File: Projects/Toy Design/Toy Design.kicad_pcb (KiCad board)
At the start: 2 copper layers, 34 parts, among them J1 Conn_01x01_Pin, J2 Conn_01x01_Pin, U1 TLV61048DBVR, U2 MCP73123, U3 NCP1117-5.0_SOT223, U4 MLX90333, U5 MLX90333, U6 MLX90333, U7 LMC6484, U8 LMC6484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

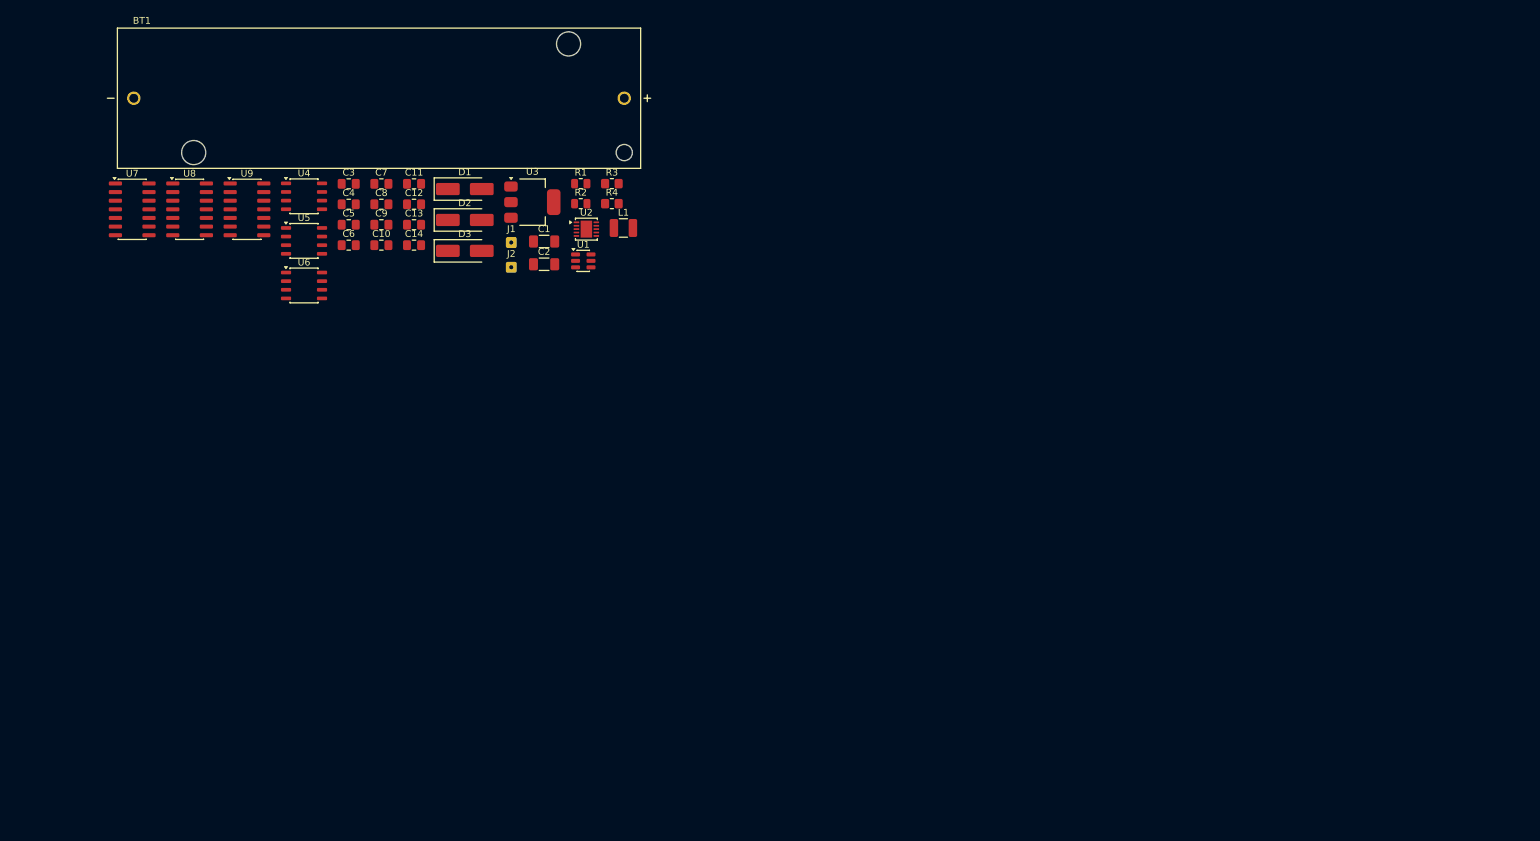
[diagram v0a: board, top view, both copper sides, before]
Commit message: Updates
Began PCB Layout and added LED controls and 3.3 to 5V level shifter
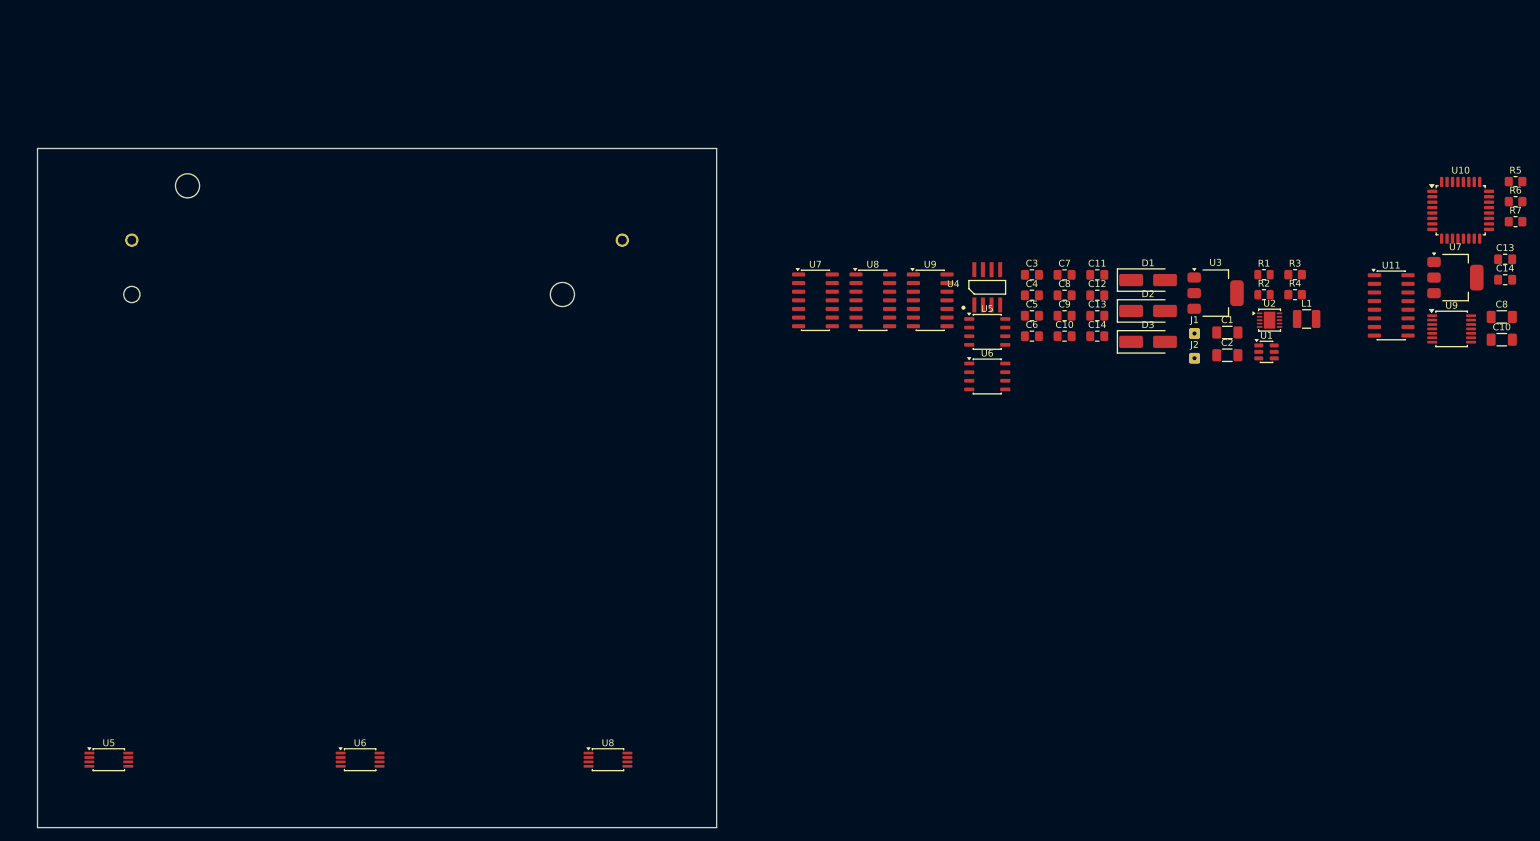
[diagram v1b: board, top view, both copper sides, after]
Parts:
- added C10: 10uF, Capacitor_SMD:C_1206_3216Metric_Pad1.33x1.80mm_HandSolder, F.Cu at (315.6, 78.2)
- added C13: 100nF, Capacitor_SMD:C_0805_2012Metric_Pad1.18x1.45mm_HandSolder, F.Cu at (316.1, 66.3)
- added C14: 100nF, Capacitor_SMD:C_0805_2012Metric_Pad1.18x1.45mm_HandSolder, F.Cu at (316.1, 69.3)
- added C8: 10uF, Capacitor_SMD:C_1206_3216Metric_Pad1.33x1.80mm_HandSolder, F.Cu at (315.6, 74.8)
- added R5: 10k, Resistor_SMD:R_0805_2012Metric_Pad1.20x1.40mm_HandSolder, F.Cu at (317.6, 54.9)
- added R6: 10k, Resistor_SMD:R_0805_2012Metric_Pad1.20x1.40mm_HandSolder, F.Cu at (317.6, 57.8)
- added R7: 10k, Resistor_SMD:R_0805_2012Metric_Pad1.20x1.40mm_HandSolder, F.Cu at (317.6, 60.8)
- added U10: STM32G030K6T6, Package_QFP:LQFP-32_7x7mm_P0.8mm, F.Cu at (309.6, 59.1)
- added U11: MCP3208-CI/SL, Package_SO:SOIC-16_3.9x9.9mm_P1.27mm, F.Cu at (299.3, 73.1)
- added U5: A1330, Package_SO:TSSOP-8_4.4x3mm_P0.65mm, F.Cu at (110.5, 140.0)
- added U6: A1330, Package_SO:TSSOP-8_4.4x3mm_P0.65mm, F.Cu at (147.5, 140.0)
- added U7: NCP1117-3.3_SOT223, Package_TO_SOT_SMD:SOT-223-3_TabPin2, F.Cu at (308.8, 69.0)
- added U8: A1330, Package_SO:TSSOP-8_4.4x3mm_P0.65mm, F.Cu at (184.0, 140.0)
- added U9: TXU0104, Package_SO:TSSOP-14_4.4x5mm_P0.65mm, F.Cu at (308.2, 76.6)
- BT1: moved to B.Cu
- U4: footprint Package_SO:JEITA_SOIC-8_3.9x4.9mm_P1.27mm -> ToyDesign:SOIC-8
- moved C1 101.5 mm to (275.2, 77.1)
- moved C10 101.5 mm to (251.2, 77.6)
- moved C2 101.5 mm to (275.2, 80.4)
- moved C3 101.5 mm to (246.4, 68.6)
- moved C4 101.5 mm to (246.4, 71.6)
- moved C5 101.5 mm to (246.4, 74.6)
- moved C6 101.5 mm to (246.4, 77.6)
- moved C7 101.5 mm to (251.2, 68.6)
- moved C8 101.5 mm to (251.2, 71.6)
- moved C9 101.5 mm to (251.2, 74.6)
- moved D1 101.5 mm to (263.5, 69.4)
- moved D2 101.5 mm to (263.5, 73.9)
- moved D3 101.5 mm to (263.5, 78.5)
- moved L1 101.5 mm to (286.9, 75.1)
- moved U7 101.5 mm to (214.5, 72.4)
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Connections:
- C12 pad 1: OUT2_U6 -> OUT_U6
- C9 pad 1: OUT1_U5 -> OUT_U5
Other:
- board outline added: 100 x 100 mm

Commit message: started pcb post led bar
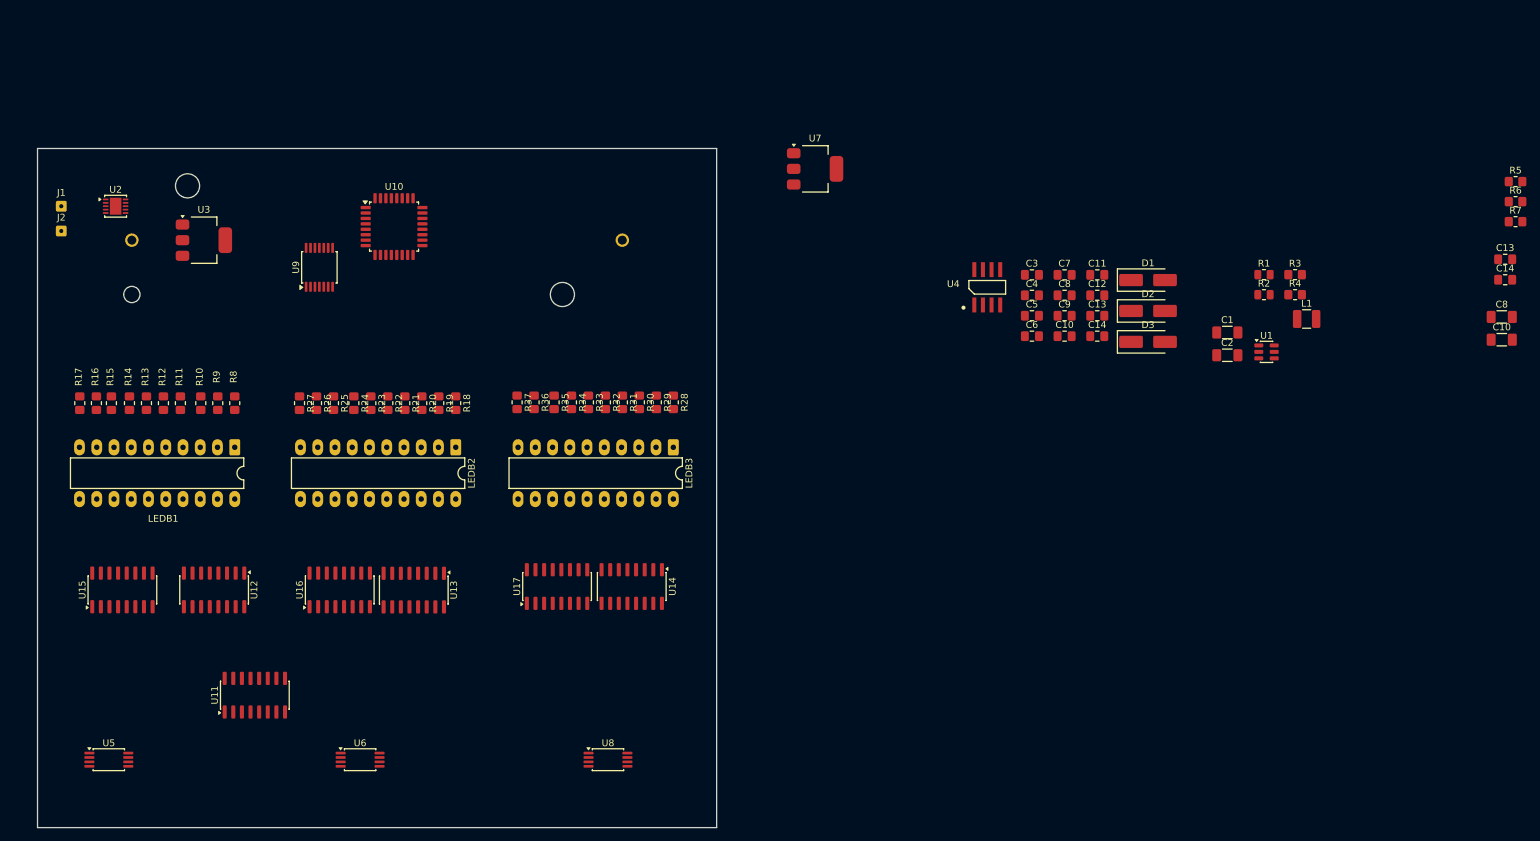
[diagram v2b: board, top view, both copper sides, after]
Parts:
- removed the U5 at (239.8, 77.0)
- removed the U6 at (239.8, 83.6)
- removed the U7 at (214.5, 72.4)
- removed the U8 at (223.0, 72.4)
- removed the U9 at (231.4, 72.4)
- added LEDB1: ~, Package_DIP:DIP-20_W7.62mm_LongPads, F.Cu at (129.0, 94.0)
- added LEDB2: ~, Package_DIP:DIP-20_W7.62mm_LongPads, F.Cu at (161.6, 94.0)
- added LEDB3: ~, Package_DIP:DIP-20_W7.62mm_LongPads, F.Cu at (193.6, 94.0)
- added R10: 1.2k, Resistor_SMD:R_0805_2012Metric_Pad1.20x1.40mm_HandSolder, F.Cu at (124.0, 87.5)
- added R11: 1.2k, Resistor_SMD:R_0805_2012Metric_Pad1.20x1.40mm_HandSolder, F.Cu at (121.0, 87.5)
- added R12: 1.2k, Resistor_SMD:R_0805_2012Metric_Pad1.20x1.40mm_HandSolder, F.Cu at (118.5, 87.5)
- added R13: 1.2k, Resistor_SMD:R_0805_2012Metric_Pad1.20x1.40mm_HandSolder, F.Cu at (116.0, 87.5)
- added R14: 1.2k, Resistor_SMD:R_0805_2012Metric_Pad1.20x1.40mm_HandSolder, F.Cu at (113.5, 87.5)
- added R15: 1.2k, Resistor_SMD:R_0805_2012Metric_Pad1.20x1.40mm_HandSolder, F.Cu at (110.9, 87.5)
- added R16: 1.2k, Resistor_SMD:R_0805_2012Metric_Pad1.20x1.40mm_HandSolder, F.Cu at (108.7, 87.5)
- added R17: 1.2k, Resistor_SMD:R_0805_2012Metric_Pad1.20x1.40mm_HandSolder, F.Cu at (106.2, 87.5)
- added R18: 1.2k, Resistor_SMD:R_0805_2012Metric_Pad1.20x1.40mm_HandSolder, F.Cu at (161.6, 87.5)
- added R19: 1.2k, Resistor_SMD:R_0805_2012Metric_Pad1.20x1.40mm_HandSolder, F.Cu at (159.1, 87.5)
- added R20: 1.2k, Resistor_SMD:R_0805_2012Metric_Pad1.20x1.40mm_HandSolder, F.Cu at (156.6, 87.5)
- added R21: 1.2k, Resistor_SMD:R_0805_2012Metric_Pad1.20x1.40mm_HandSolder, F.Cu at (154.1, 87.5)
- added R22: 1.2k, Resistor_SMD:R_0805_2012Metric_Pad1.20x1.40mm_HandSolder, F.Cu at (151.6, 87.5)
- added R23: 1.2k, Resistor_SMD:R_0805_2012Metric_Pad1.20x1.40mm_HandSolder, F.Cu at (149.1, 87.5)
- added R24: 1.2k, Resistor_SMD:R_0805_2012Metric_Pad1.20x1.40mm_HandSolder, F.Cu at (146.6, 87.5)
- added R25: 1.2k, Resistor_SMD:R_0805_2012Metric_Pad1.20x1.40mm_HandSolder, F.Cu at (143.6, 87.5)
- added R26: 1.2k, Resistor_SMD:R_0805_2012Metric_Pad1.20x1.40mm_HandSolder, F.Cu at (141.1, 87.5)
- added R27: 1.2k, Resistor_SMD:R_0805_2012Metric_Pad1.20x1.40mm_HandSolder, F.Cu at (138.6, 87.5)
- added R28: 1.2k, Resistor_SMD:R_0805_2012Metric_Pad1.20x1.40mm_HandSolder, F.Cu at (193.6, 87.4)
- added R29: 1.2k, Resistor_SMD:R_0805_2012Metric_Pad1.20x1.40mm_HandSolder, F.Cu at (191.1, 87.4)
- added R30: 1.2k, Resistor_SMD:R_0805_2012Metric_Pad1.20x1.40mm_HandSolder, F.Cu at (188.6, 87.4)
- added R31: 1.2k, Resistor_SMD:R_0805_2012Metric_Pad1.20x1.40mm_HandSolder, F.Cu at (186.1, 87.4)
- added R32: 1.2k, Resistor_SMD:R_0805_2012Metric_Pad1.20x1.40mm_HandSolder, F.Cu at (183.6, 87.4)
- added R33: 1.2k, Resistor_SMD:R_0805_2012Metric_Pad1.20x1.40mm_HandSolder, F.Cu at (181.1, 87.4)
- added R34: 1.2k, Resistor_SMD:R_0805_2012Metric_Pad1.20x1.40mm_HandSolder, F.Cu at (178.6, 87.4)
- added R35: 1.2k, Resistor_SMD:R_0805_2012Metric_Pad1.20x1.40mm_HandSolder, F.Cu at (176.1, 87.4)
- added R36: 1.2k, Resistor_SMD:R_0805_2012Metric_Pad1.20x1.40mm_HandSolder, F.Cu at (173.1, 87.4)
- added R37: 1.2k, Resistor_SMD:R_0805_2012Metric_Pad1.20x1.40mm_HandSolder, F.Cu at (170.6, 87.4)
- added R8: 1.2k, Resistor_SMD:R_0805_2012Metric_Pad1.20x1.40mm_HandSolder, F.Cu at (129.0, 87.5)
- added R9: 1.2k, Resistor_SMD:R_0805_2012Metric_Pad1.20x1.40mm_HandSolder, F.Cu at (126.5, 87.5)
- added U12: 74HC595, Package_SO:SOIC-16_3.9x9.9mm_P1.27mm, F.Cu at (126.0, 115.0)
- added U13: 74HC595, Package_SO:SOIC-16_3.9x9.9mm_P1.27mm, F.Cu at (155.4, 115.0)
- added U14: 74HC595, Package_SO:SOIC-16_3.9x9.9mm_P1.27mm, F.Cu at (187.5, 114.5)
- added U15: 74HC595, Package_SO:SOIC-16_3.9x9.9mm_P1.27mm, F.Cu at (112.5, 115.0)
- added U16: 74HC595, Package_SO:SOIC-16_3.9x9.9mm_P1.27mm, F.Cu at (144.5, 115.0)
- added U17: 74HC595, Package_SO:SOIC-16_3.9x9.9mm_P1.27mm, F.Cu at (176.5, 114.5)
- moved U11 176.9 mm to (132.0, 130.5), turned to 90 degrees
- moved U2 170.7 mm to (111.5, 58.5)
- moved J1 167.9 mm to (103.5, 58.5)
- moved J2 167.9 mm to (103.5, 62.1)
- moved U9 167.0 mm to (141.5, 67.5), turned to 90 degrees
- moved U10 157.1 mm to (152.5, 61.5)
- moved U3 149.2 mm to (124.5, 63.5)
- moved U7 95.6 mm to (214.5, 53.0)
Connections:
- BT1 pad N: unconnected-(BT1-PadN) -> GND
- U10 pad 28: unconnected-(U10-PB4-Pad28) -> RCLK_LED
- U10 pad 29: unconnected-(U10-PB5-Pad29) -> ~{SRCLR}
- U10 pad 31: unconnected-(U10-PB7-Pad31) -> SPI2_MOSI_LED
- U10 pad 32: unconnected-(U10-PB8-Pad32) -> SPI2_SCK_LED

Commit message: Update to commit to main
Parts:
- moved J2 0.85 mm to (103.5, 63.0)
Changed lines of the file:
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@@
 	(footprint "Connector_Wire:SolderWire-0.1sqmm_1x01_D0.4mm_OD1mm"
 		(layer "F.Cu")
-		(at 103.5 62.15)
+		(at 103.5 63)
 		(descr "Soldered wire connection, for a single 0.1 mm² wire, basic insulation, conductor diameter 0.4mm, outer diameter 1mm, size source Multi-Contact FLEXI-E 0.10 (https://www.staubli.com/content/dam/ecs/catalogs-brochures/TM/CAB-Main-11014119-en.pdf#page=9), bend radius 3 times outer diameter, generated with kicad-footprint-generator")
 		(tags "connector wire 0.1sqmm")
